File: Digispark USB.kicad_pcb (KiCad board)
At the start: 2 copper layers, 40 x 13.5 mm, 12 parts, among them J1 Conn_01x04, J2 Conn_01x04, U2 ATtiny85-20S

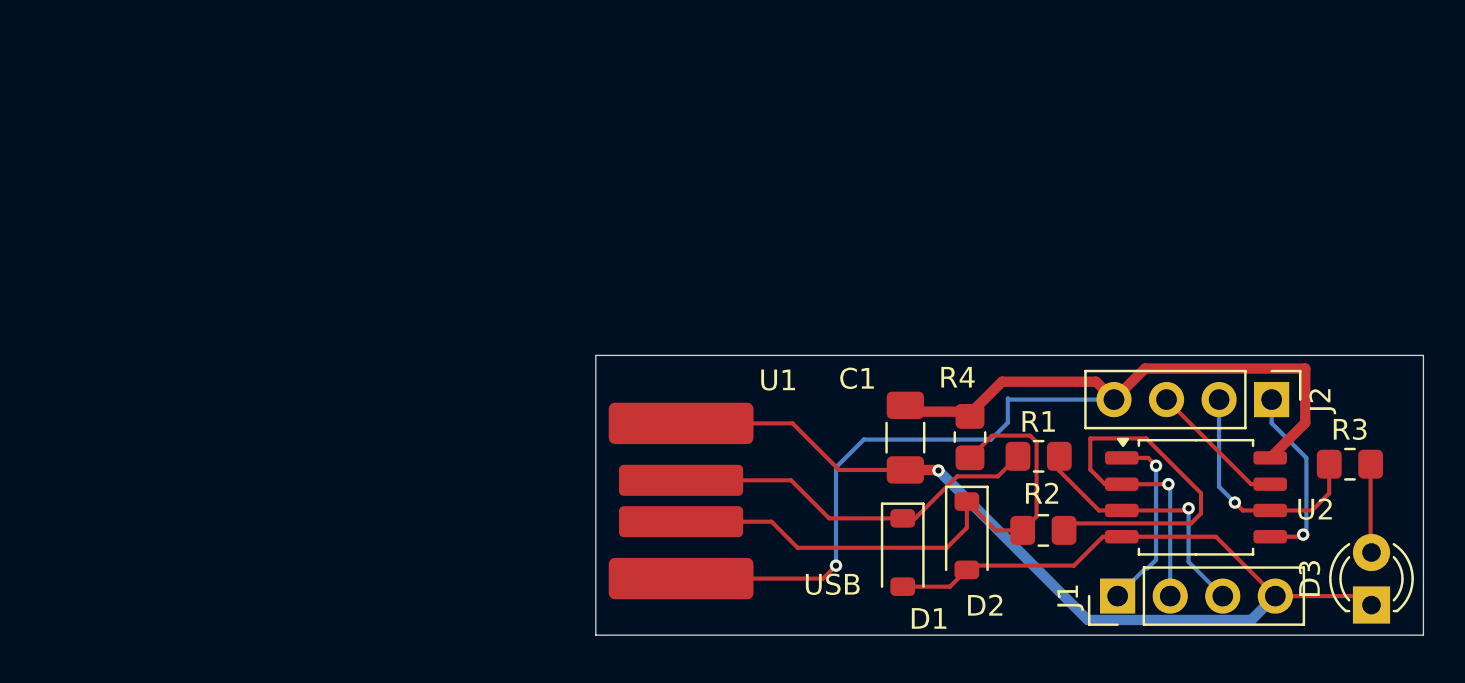
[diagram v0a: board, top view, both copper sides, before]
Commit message: Update PCB layout, remove panel files, add gitignore for backups
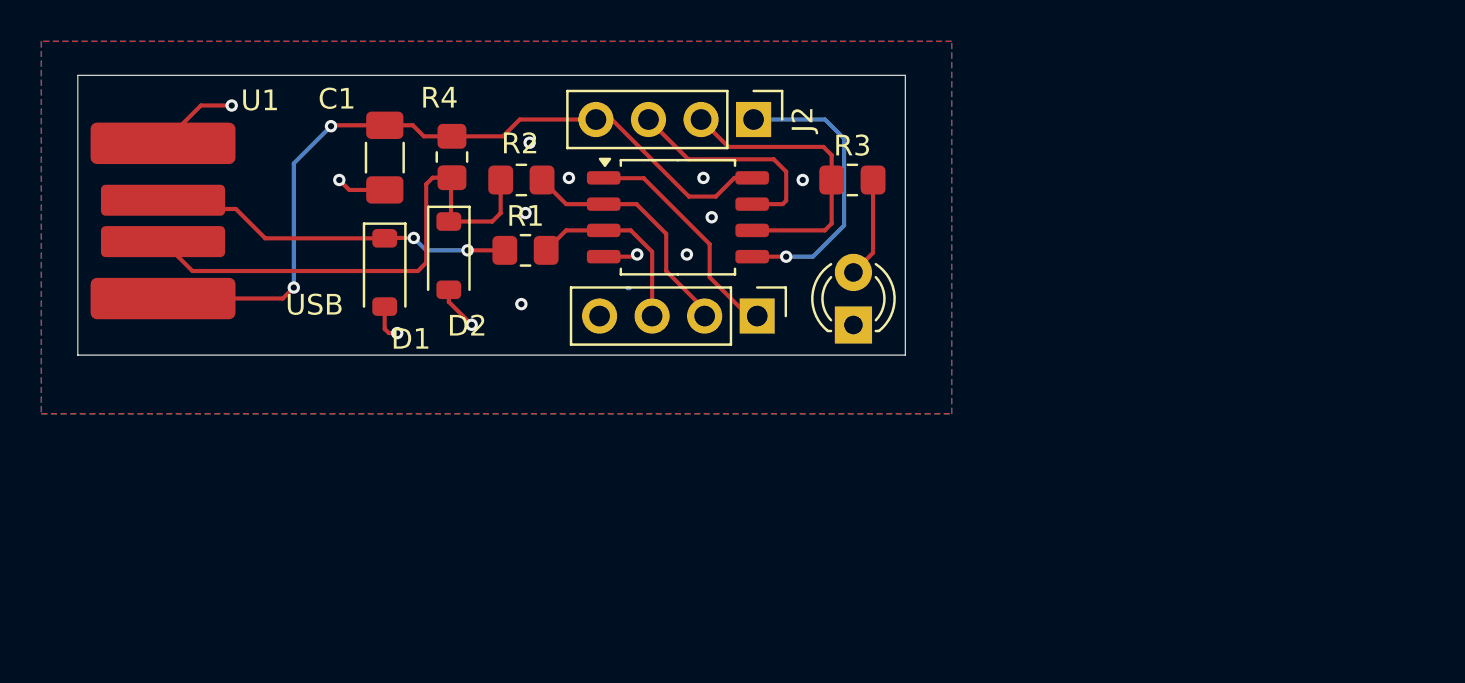
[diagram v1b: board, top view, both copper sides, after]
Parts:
- moved R2 30.4 mm to (123.4, 68.0)
- moved C1 28.6 mm to (116.8, 66.9)
- moved D2 28.5 mm to (119.9, 71.7)
- moved R4 28.5 mm to (120.0, 66.9)
- moved U1 28.5 mm to (106.1, 70.0)
- moved J2 28.5 mm to (134.6, 65.1)
- moved U2 28.5 mm to (131.0, 69.8)
- moved D1 28.5 mm to (116.8, 72.5)
- moved D3 28.5 mm to (139.5, 75.0)
- moved R3 27.7 mm to (139.4, 68.0)
- moved R1 26.7 mm to (123.6, 71.4)
- moved J1 22.1 mm to (134.8, 74.6), turned to -90 degrees
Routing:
- net GND: track 58.2 -> 13.0 mm, vias 1 -> 13
- net +5V: track 54.3 -> 38.8 mm, vias 1 -> 2
- net Net-(J1-Pin_2): track 25.7 -> 11.8 mm, vias 1 -> 0
- net Net-(J2-Pin_1): track 8.92 -> 14.0 mm
- net Net-(J2-Pin_3): track 6.70 -> 10.8 mm
- net Net-(J1-Pin_3): track 12.7 -> 9.05 mm, vias 1 -> 0
- net Net-(D2-K): track 27.9 -> 25.1 mm
- net Net-(J2-Pin_2): track 11.8 -> 14.3 mm, vias 1 -> 0
- net Net-(J1-Pin_1): track 8.94 -> 11.2 mm, vias 1 -> 0
- net Net-(D1-K): track 18.3 -> 17.5 mm, vias 0 -> 2
- net Net-(D3-A): track 4.28 -> 4.92 mm
- added copper zone on B.Cu, net GND
- added copper zone on F.Cu, net GND
